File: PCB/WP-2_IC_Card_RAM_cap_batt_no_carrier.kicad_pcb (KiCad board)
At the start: 2 copper layers, 45 x 54 mm, 11 parts, among them J1 Conn_01x38_Female, U1 SRAM 128Kx8 5v Parallel, U2 SRAM 128Kx8 5v Parallel

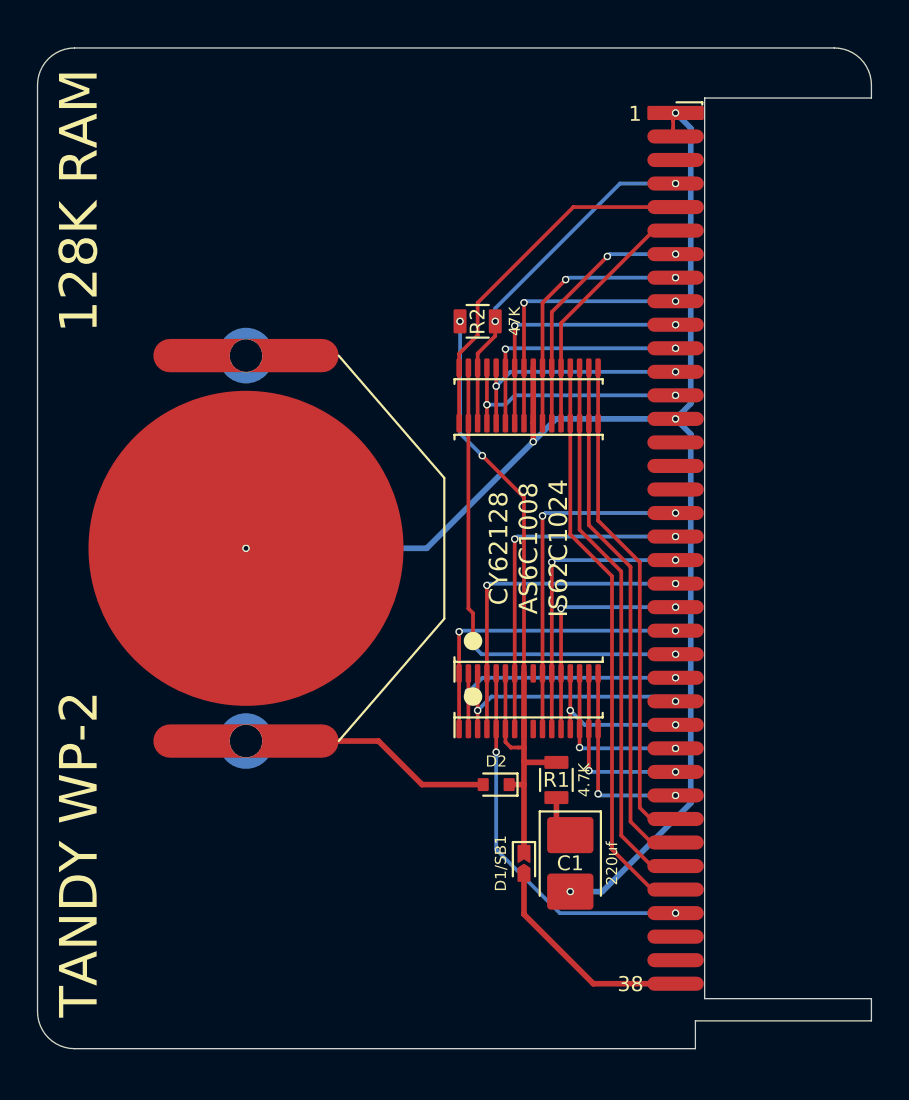
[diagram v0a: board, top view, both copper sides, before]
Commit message: fine-tune via-near-trace placements
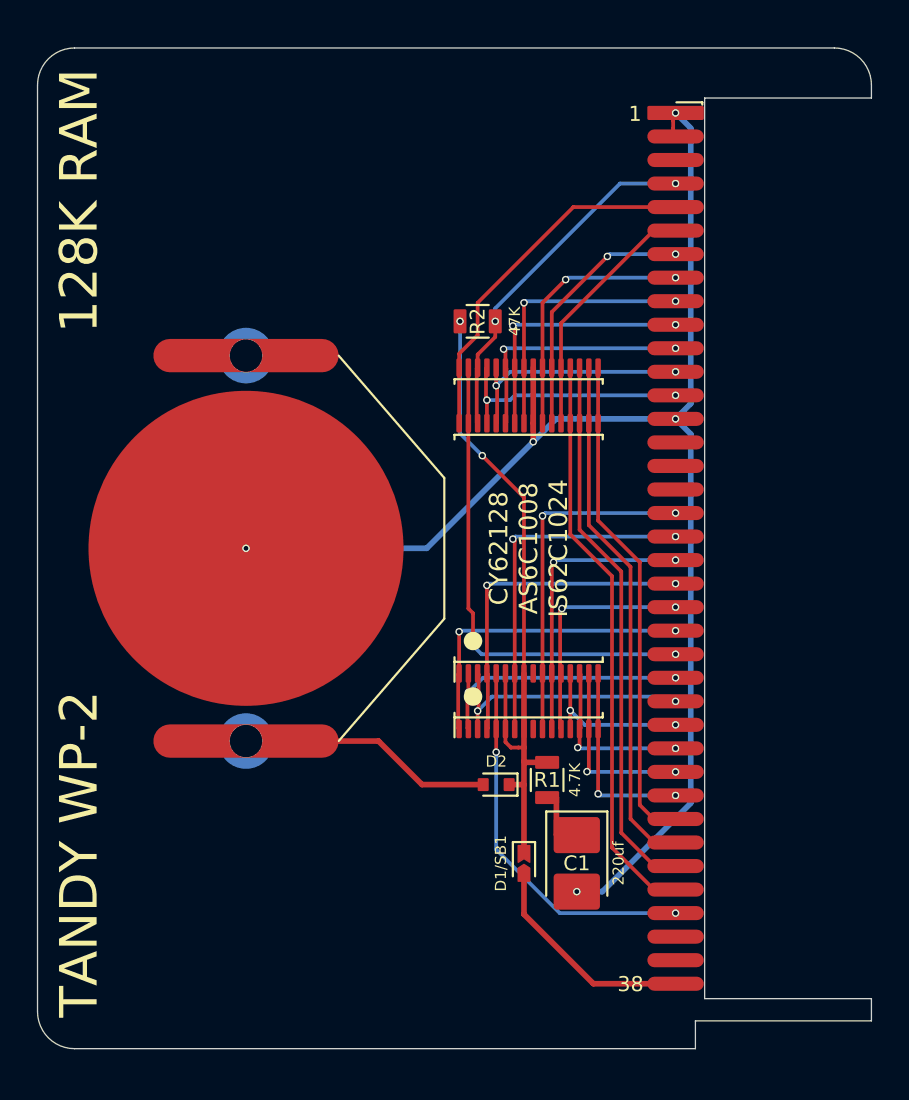
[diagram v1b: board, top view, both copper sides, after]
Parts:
- moved R1 0.50 mm to (150.2, 112.2)
- moved C1 0.35 mm to (151.8, 116.7)
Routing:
- net Net-(C1-Pad1): track 2.34 -> 3.61 mm
- net VMEM: track 32.8 -> 32.3 mm

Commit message: increase via sizes and min soldermask width for PCBWAY
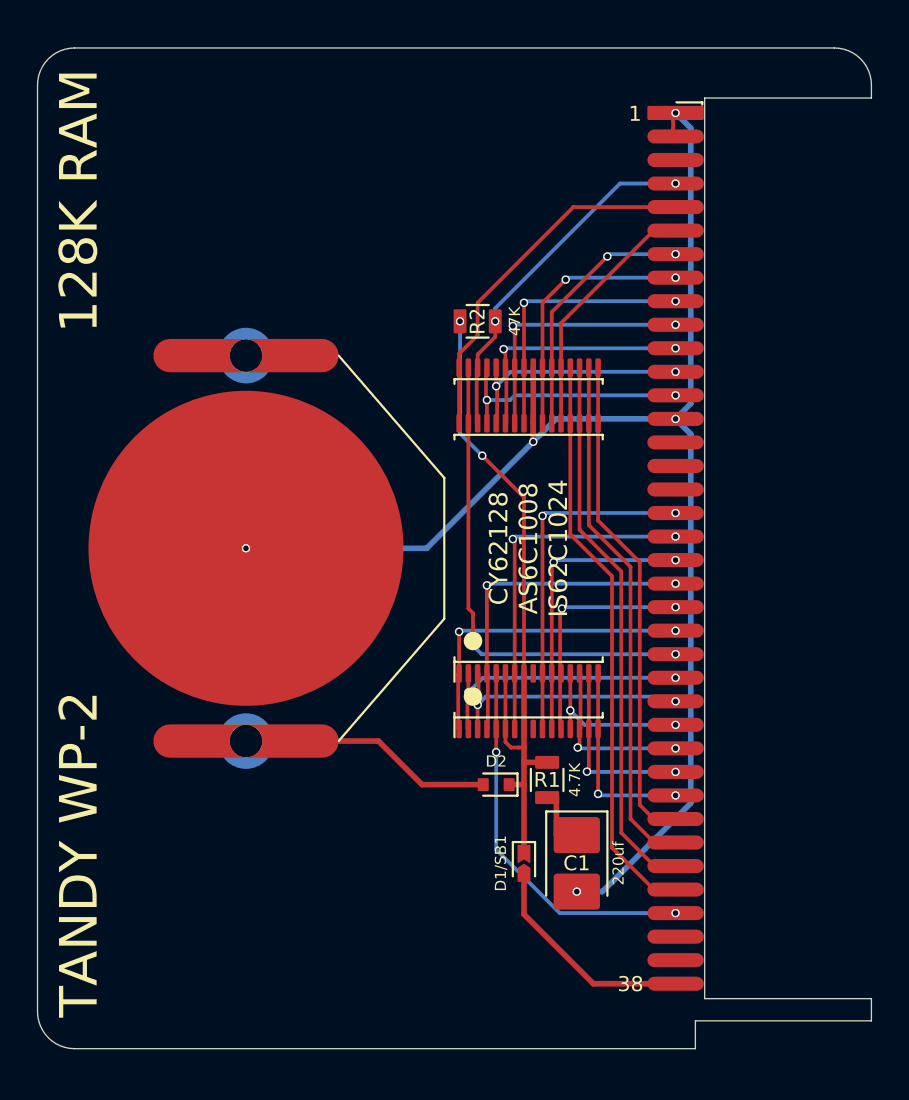
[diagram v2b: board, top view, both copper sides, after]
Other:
- net class Default: trace_width 0.254 -> 0.18; via_dia 0.4064 -> 0.46; via_drill 0.254 -> 0.3
- rule via_min_drill: 0.254 -> 0.3
- rule via_min_size: 0.4064 -> 0.46
